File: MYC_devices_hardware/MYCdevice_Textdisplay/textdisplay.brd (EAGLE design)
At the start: 61 x 39.4 mm, 25 parts, among them IC1 MEGA8-P, IC2 78L05, Q1 20MHz, Q2 BC307, X1 8-15V, X2 1503_09, X3 1503_09

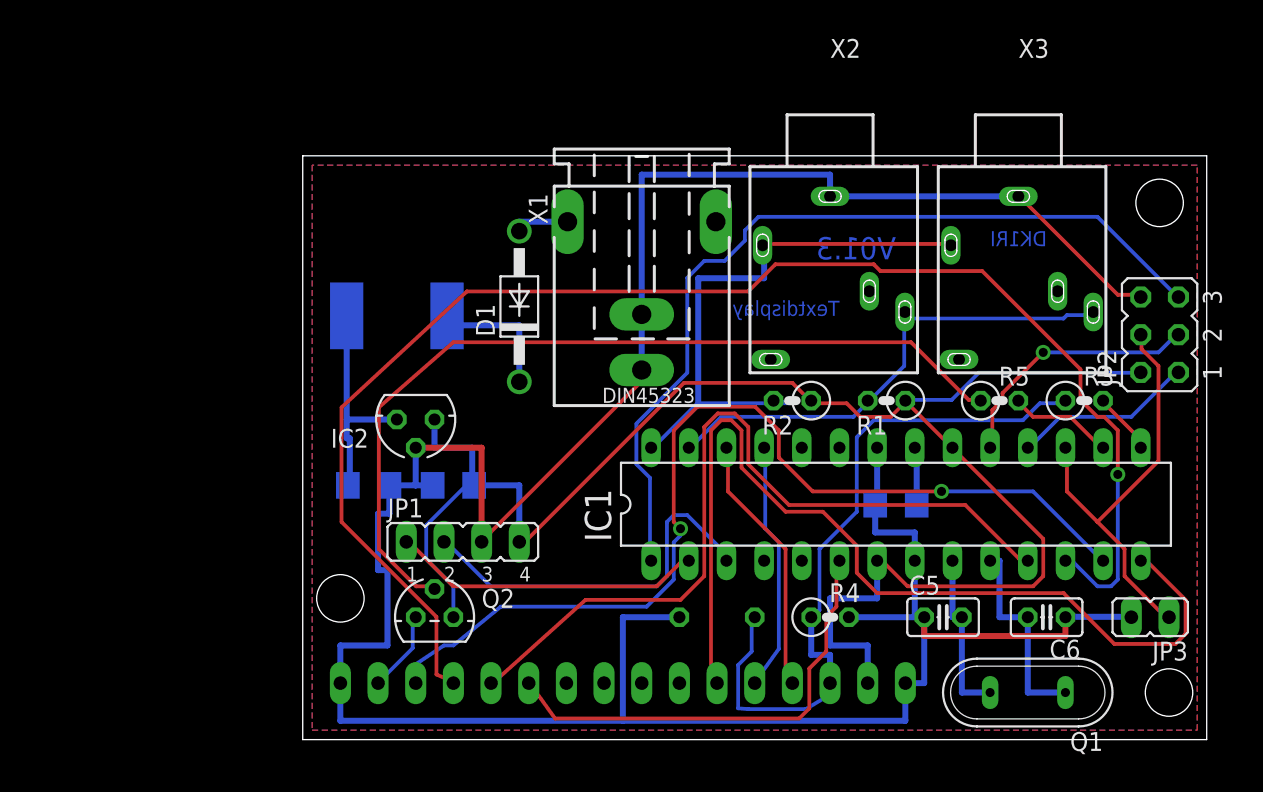
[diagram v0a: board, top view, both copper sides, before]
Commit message: now with includefiles, new board
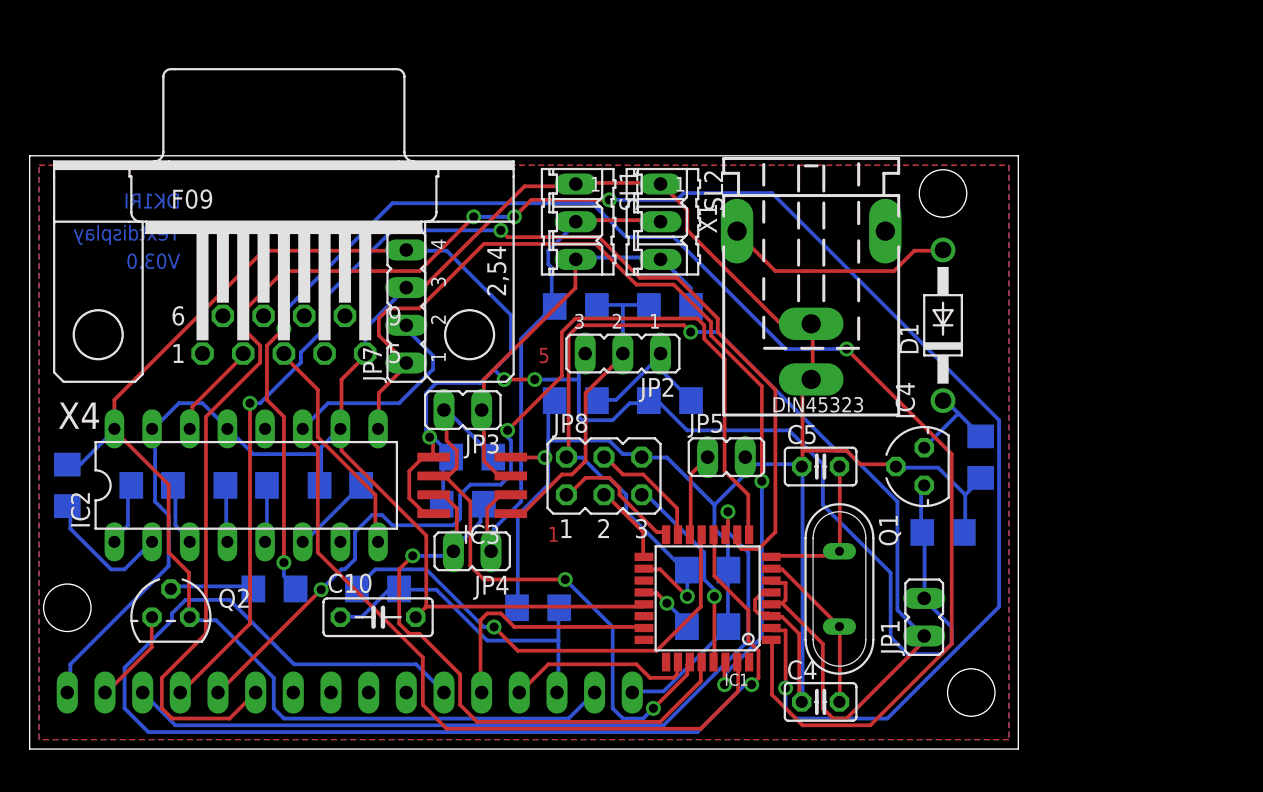
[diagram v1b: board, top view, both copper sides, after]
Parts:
- removed L1: 22u, inductor-neosid:MS85
- removed X2, X3: 1503_09, con-lumberg:1503_09
- added C10: 100n, resistor:C050-025X075
- added C11, C3, C8, C9: 22u, resistor:C1206
- added IC3: PCA9517, PCA9517:SO-08
- added IC4: 78L05, v-reg:78LXX
- added JP4: SCL, jumper:JP1
- added JP5: Reset, jumper:JP1
- added JP7: USB, jumper:JP4
- added JP8: ISP, jumper:JP3Q
- added R6: 1k5, resistor:R1206
- added R7: 1k, resistor:R1206
- added R8: 4k7, resistor:R1206
- added R9: 10k, resistor:R1206
- added SL3: SL3, con-amp-quick:08P
- added SL4: SL4, con-amp-quick:08P
- added X4: RS232, con-subd:F09H
- C4: value 22u -> 18pF; device resistor:C1206 -> resistor:C025-025X050
- C6: value 18pF -> 22u; device resistor:C025-025X050 -> resistor:C1206
- C7: value 100n -> 22u; device resistor:C050-025X075 -> resistor:C1206
- IC1: value MEGA8-P -> MEGA168; device atmel:DIL28-3 -> atmel:TQFP32-08
- IC2: value 78L05 -> MAX232; device v-reg:78LXX -> maxim:DIL16
- JP1: value USB -> Power; device jumper:JP4 -> jumper:JP1
- JP2: value ISP -> 3V/5V; device jumper:JP3Q -> jumper:JP2
- JP3: value Reset -> SDA
- R1, R2: value 4k7 -> see manual; device resistor:0207/2V -> resistor:R1206
- R3: value 1k -> see manual; device resistor:0207/2V -> resistor:R1206
- R4: value 10k -> see manual; device resistor:0207/2V -> resistor:R1206
- R5: value 4k7 -> 1k; device resistor:0207/2V -> resistor:R1206
- SL1: value SL1 -> I2C; device con-amp-quick:08P -> con-amp-quick:03P
- SL2: value SL2 -> I2C; device con-amp-quick:08P -> con-amp-quick:03P
- moved C6 61.0 mm to (8.26, 17.8), flipped to the bottom
- moved JP3 48.4 mm to (29.2, 22.9)
- moved R3 41.5 mm to (29.8, 19.7), flipped to the bottom, turned to 180 degrees
- moved C1 41.3 mm to (64.1, 19.7), turned to 270 degrees
- moved JP2 36.2 mm to (40.0, 26.7), turned to 180 degrees
- moved SL1 33.9 mm to (36.8, 35.6), flipped to the top, turned to 270 degrees
- moved SL2 33.6 mm to (42.5, 35.6), flipped to the top, turned to 270 degrees
- moved C2 33.2 mm to (61.6, 14.6), turned to 180 degrees
- moved C7 33.0 mm to (14.6, 17.8), turned to 180 degrees
- moved JP1 31.5 mm to (60.3, 8.89)
- moved D1 28.6 mm to (61.6, 28.6)
- moved R4 25.9 mm to (29.2, 16.5), flipped to the bottom, turned to 180 degrees
- moved R5 22.2 mm to (43.2, 23.5), flipped to the bottom
- moved Q2 17.8 mm to (9.53, 8.89)
- moved R2 15.9 mm to (36.8, 29.8), flipped to the bottom, turned to 0 degrees
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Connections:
- new net N$11: C9.1, IC2.6
- new net N$12: C8.2, IC2.2
- new net N$13: C6.1, IC2.1
- new net N$14: IC2.8, X4.3
- new net N$15: IC2.14, X4.2
- new net N$16: IC1.14, JP5.1
- new net N$24: IC3.1, JP2.2, R1.1, R2.1
- new net N$3: IC3.3, JP3.1, R1.2, SL1.3, SL2.3
- new net N$5: IC3.2, JP4.1, R2.2, SL1.2, SL2.2
- new net N$6: C11.2, IC1.18, IC1.4, IC1.6, JP1.1, JP8.2
- new net N$7: C6.2, IC2.3
- new net N$8: C7.1, IC2.4
- new net N$9: C7.2, IC2.5
- net -: now also IC1.13, R7.2; no longer IC1.15, R3.2
- net BRIGHT: now also SL4.7; no longer SL2.7
- net CONTRAST: now also C10.1, R7.1, R9.1, SL3.3; no longer C7.1, R3.1, R4.1, SL1.3
- net D4: now also IC1.2, SL4.3; no longer IC1.6, SL2.3
- net D5: now also IC1.9, SL4.4; no longer IC1.11, SL2.4
- net D6: now also IC1.10, SL4.5; no longer IC1.12, SL2.5
- net D7: now also IC1.11, SL4.6; no longer IC1.13, SL2.6
- net E: now also IC1.12, SL3.6; no longer IC1.14, SL1.6
- net GND: now also C10.2, C11.1, C3.1, C9.2, IC1.21, IC1.3, IC1.5, IC2.10, IC2.13, IC2.15, IC3.4, IC4.GND, JP5.2, JP7.3, JP8.6, R6.1, R9.2, SL2.1, SL3.1, SL4.8, X4.5; no longer C6.1, C7.2, IC1.22, IC1.8, IC2.GND, JP1.3, JP2.6, JP3.2, R4.2, SL2.8, X2.1, X3.1
- net MISO: now also IC1.16, JP8.1; no longer IC1.18, JP2.1
- net MOSI: now also IC1.15, JP8.4; no longer IC1.17, JP2.4, JP3.1
- net N$1: now also JP2.1, R5.1, R6.2; no longer D1.C, L1.1
- net N$18: now also D1.C, IC4.IN; no longer IC2.IN, L1.2
- net N$19: now also C4.2, IC1.7; no longer C5.2, IC1.9
- net N$2: now also IC1.1, R8.2; no longer IC1.16, R5.2
- net N$35: now also C3.2, IC1.20; no longer C4.2, IC1.21
- net N$37: now also C5.2, IC1.8; no longer C6.2, IC1.10
- net N$4: now also R8.1; no longer R5.1
- net R/W: now also IC1.23, SL3.5; no longer IC1.25, SL1.5
- net RESET: now also IC1.29, JP8.5; no longer IC1.1, JP2.5
- net RS: now also SL3.4; no longer SL1.4
- net RXD: now also IC1.30, IC2.9, JP7.1; no longer IC1.2, JP1.1
- net SCK: now also IC1.17, JP8.3; no longer IC1.19, JP2.3
- net SCL: now also IC3.7, JP4.2, R4.2; no longer R2.2, X2.2, X3.2
- net SDA: now also IC3.6, JP3.2, R3.2; no longer R1.2, X2.3, X3.3
- net TXD: now also IC1.31, IC2.11, JP7.2; no longer IC1.3, JP1.2
- net VDD: now also C8.1, IC2.16, IC3.5, IC3.8, IC4.OUT, JP1.2, JP2.3, JP7.4, R3.1, R4.1, R5.2, SL3.2; no longer IC1.20, IC1.7, IC2.OUT, JP1.4, JP2.2, R1.1, R2.1, SL1.2
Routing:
- net D4: track 31.2 -> 134.5 mm, vias 0 -> 4
- net N$2: track 7.07 -> 106.8 mm, vias 0 -> 3
- net N$6: track 0.00 -> 84.1 mm, vias 0 -> 2
- net VDD: track 116.0 -> 170.7 mm, vias 0 -> 3
- net N$4: track 58.3 -> 5.86 mm
- net RESET: track 58.4 -> 13.5 mm, vias 0 -> 1
- net RXD: track 21.0 -> 64.1 mm, vias 0 -> 2
- net N$5: track 0.00 -> 35.8 mm
- net TXD: track 25.9 -> 61.3 mm
- net N$3: track 0.00 -> 28.4 mm
- net -: track 4.29 -> 32.1 mm, vias 0 -> 1
- net GND: track 197.7 -> 224.6 mm, vias 0 -> 1
- net CONTRAST: track 48.1 -> 22.7 mm
- net N$24: track 0.00 -> 21.7 mm
- net MOSI: track 29.5 -> 8.14 mm
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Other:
- board size 61 x 39.4 mm -> 66.7 x 40 mm
- board text added: "1"
- board text added: "5"
- board text added: "V03.0"
- board text removed: "V01.3"
